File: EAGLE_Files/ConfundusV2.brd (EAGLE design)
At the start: 43.8 x 20 mm, 89 parts, among them IC1 MIC5219YM5_TR, IC2 ATTINY1616-MNR, IC4 TPS61291DRVT, J5 SM03B-SRSS-TB_LF__SN_, Q1 DMG3415U-7, Q3 DMG3415U-7, SW1 MLL1200S

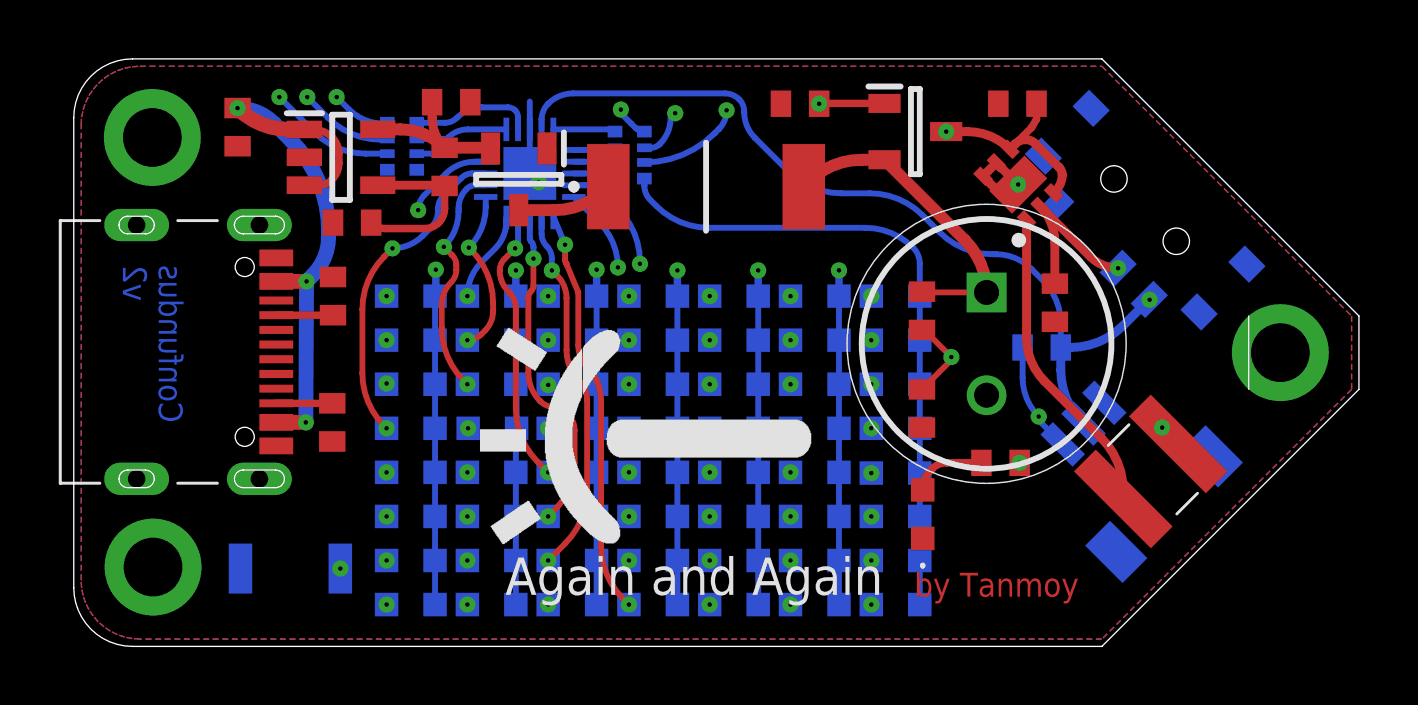
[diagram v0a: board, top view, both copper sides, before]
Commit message: Updating the circuit adjustments for introduction of a Schottky diode
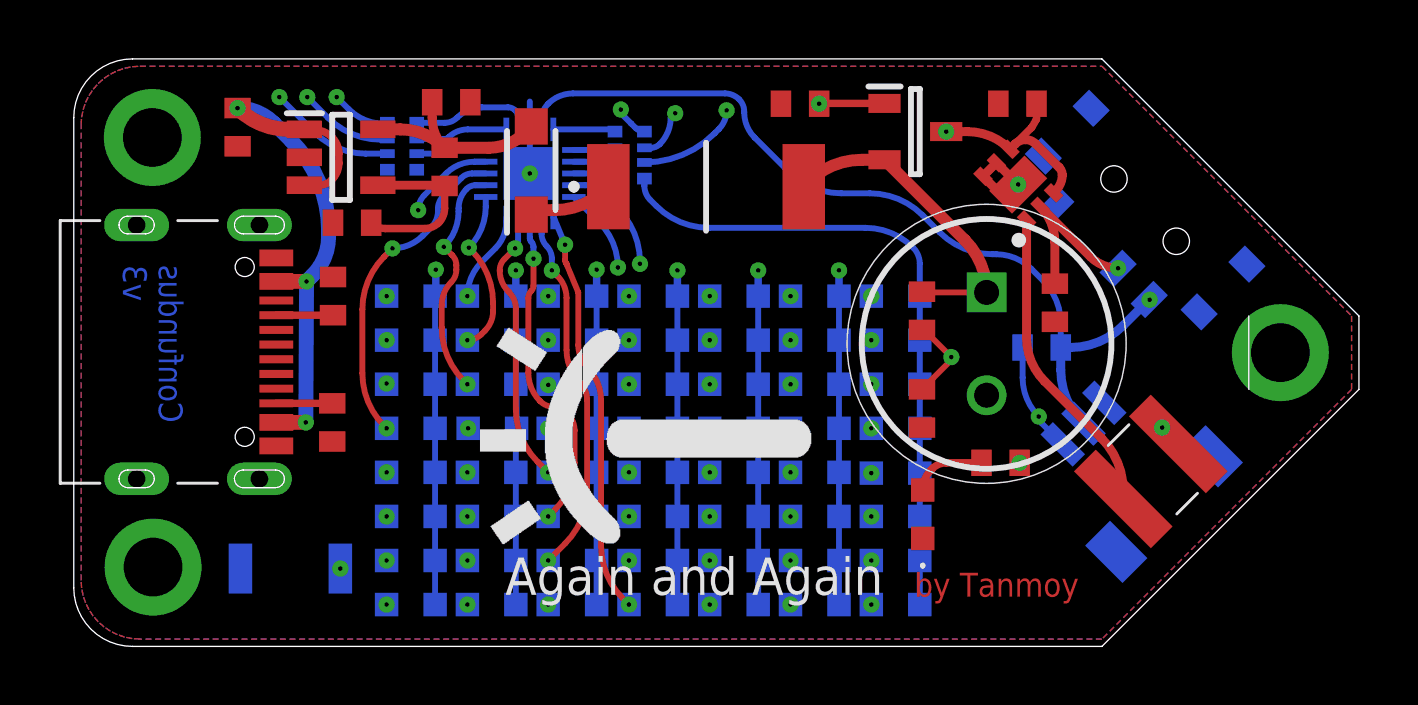
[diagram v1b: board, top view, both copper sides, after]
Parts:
- removed Q1: DMG3415U-7, DMG3415U-7:SOT96P240X100-3N
- added D1: MBR120VLSFT1G, MBR120VLSFT1G:SODFL3616X98N
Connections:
- net GND: no longer Q1.1
- net N$10: now also D1.2; no longer Q1.2
- net N$12: now also D1.1; no longer Q1.3
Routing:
- net N$10: track 5.60 -> 7.17 mm
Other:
- board text added: "Confundus v3"
- board text removed: "Confundus v2"
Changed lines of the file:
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@@
 <plain>
 <text x="3.70554375" y="12.98660625" size="0.8128" layer="16" rot="MR270">Confundus
-       v2</text>
+       v3</text>
 <text x="27.55" y="3.025" size="1.27" layer="25" rot="R180">Again and Again</text>
 <wire x1="35" y1="20" x2="2" y2="20" width="0.001" layer="20"/>
@@
 <attribute name="MOUSER_PRICE-STOCK" value="" x="9.1" y="16.65" size="1.778" layer="27" display="off"/>
 </element>
-<element name="Q1" library="DMG3415U-7" package="SOT96P240X100-3N" override_package3d_urn="urn:adsk.eagle:package:51305947/2" override_package_urn="urn:adsk.eagle:footprint:51305948/1" value="DMG3415U-7" x="15.15" y="15.9" smashed="yes" rot="R270">
-<attribute name="DESCRIPTION" value="P-CHANNEL ENHANCEMENT MODE MOSFET" x="15.15" y="15.9" size="1.778" layer="27" rot="R270" display="off"/>
-<attribute name="HEIGHT" value="1mm" x="15.15" y="15.9" size="1.778" layer="27" rot="R270" display="off"/>
-<attribute name="LCSC_PART_NUMBER" value="C96616" x="15.15" y="15.9" size="1.778" layer="27" rot="R270" display="off"/>
-<attribute name="LCSC_PRICE-STOCK" value="https://lcsc.com/product-detail/MOSFET_Diodes-Incorporated_DMG3415U-7_Diodes-Incorporated-DMG3415U-7_C96616.html" x="15.15" y="15.9" size="1.778" layer="27" rot="R270" display="off"/>
-<attribute name="MANUFACTURER_NAME" value="Diodes Inc." x="15.15" y="15.9" size="1.778" layer="27" rot="R270" display="off"/>
-<attribute name="MANUFACTURER_PART_NUMBER" value="DMG3415U-7" x="15.15" y="15.9" size="1.778" layer="27" rot="R270" display="off"/>
-</element>
 <element name="R4" library="ERJ1TYJ220U" package="ERJ1TRQF1R0U" override_package3d_urn="urn:adsk.eagle:package:52775042/2" override_package_urn="urn:adsk.eagle:footprint:52775043/1" value="ERJ1TYJ220U" x="21.525" y="15.65" smashed="yes">
 <attribute name="ARROW_PART_NUMBER" value="" x="21.525" y="15.65" size="1.778" layer="27" display="off"/>
@@
 <attribute name="MOUSER_PART_NUMBER" value="" x="21.525" y="15.65" size="1.778" layer="27" display="off"/>
 <attribute name="MOUSER_PRICE-STOCK" value="" x="21.525" y="15.65" size="1.778" layer="27" display="off"/>
+</element>
+<element name="D1" library="MBR120VLSFT1G" package="SODFL3616X98N" override_package3d_urn="urn:adsk.eagle:package:53013620/2" override_package_urn="urn:adsk.eagle:footprint:53013621/1" value="MBR120VLSFT1G" x="15.575" y="16.2" smashed="yes" rot="R90">
+<attribute name="DESCRIPTION" value="Diode Schottky 20V 1A SOD123FL ON Semi MBR120VLSFT1G, SMT Schottky Diode, 20V 1A, 2-Pin SOD-123FL" x="15.575" y="16.2" size="1.778" layer="27" rot="R90" display="off"/>
+<attribute name="HEIGHT" value="0.98mm" x="15.575" y="16.2" size="1.778" layer="27" rot="R90" display="off"/>
+<attribute name="MANUFACTURER_NAME" value="ON Semiconductor" x="15.575" y="16.2" size="1.778" layer="27" rot="R90" display="off"/>
+<attribute name="MANUFACTURER_PART_NUMBER" value="MBR120VLSFT1G" x="15.575" y="16.2" size="1.778" layer="27" rot="R90" display="off"/>
+<attribute name="MOUSER_PART_NUMBER" value="863-MBR120VLSFT1G" x="15.575" y="16.2" size="1.778" layer="27" rot="R90" display="off"/>
+<attribute name="MOUSER_PRICE-STOCK" value="https://www.mouser.co.uk/ProductDetail/ON-Semiconductor/MBR120VLSFT1G?qs=3JMERSakebpX%252BkItPpFCkg%3D%3D" x="15.575" y="16.2" size="1.778" layer="27" rot="R90" display="off"/>
 </element>
 </elements>
@@
 <contactref element="J3" pad="1"/>
 <contactref element="C10" pad="2"/>
-<via x="15.825" y="15.8" extent="1-16" drill="0.15" grouprefs="VIAS"/>
-<wire x1="15.525" y1="16.1" x2="15.825" y2="15.8" width="0.2032" layer="16"/>
+<via x="15.525" y="16.1" extent="1-16" drill="0.15" grouprefs="VIAS"/>
 <polygon width="0.1" layer="1">
 <vertex x="35" y="0.25"/>
@@
 <contactref element="IC1" pad="2"/>
 <contactref element="R2" pad="1"/>
-<contactref element="Q1" pad="1"/>
 <via x="32.15" y="15.725" extent="1-16" drill="0.15"/>
 <wire x1="32.15303125" y1="15.72196875" x2="32.15" y2="15.725" width="0.254" layer="1"/>
@@
 <contactref element="IC1" pad="5"/>
 <contactref element="C10" pad="1"/>
-<contactref element="Q1" pad="2"/>
 <contactref element="R1" pad="2"/>
 <wire x1="10.35" y1="17.6" x2="11.116115625" y2="17.6" width="0.4064" layer="1"/>
@@
 <wire x1="12.2" y1="18.001040625" x2="12.625" y2="16.975" width="0.3048" layer="1" curve="45"/>
 <wire x1="12.625" y1="16.975" x2="14.12964375" y2="16.975" width="0.4064" layer="1"/>
-<wire x1="14.12964375" y1="16.975" x2="14.19" y2="16.95" width="0.4064" layer="1" curve="-45"/>
+<contactref element="D1" pad="2"/>
+<wire x1="14.12964375" y1="16.975" x2="15.35936875" y2="17.48436875" width="0.4064" layer="1" curve="45"/>
+<wire x1="15.35936875" y1="17.48436875" x2="15.575" y2="17.7" width="0.4064" layer="1"/>
 </signal>
 <signal name="N$12">
-<contactref element="Q1" pad="3"/>
 <contactref element="R4" pad="1"/>
-<wire x1="15.15" y1="14.85" x2="16.347896875" y2="14.85" width="0.4064" layer="1"/>
-<wire x1="16.347896875" y1="14.85" x2="18.14395" y2="15.59395" width="0.4064" layer="1" curve="45"/>
+<wire x1="18.14395" y1="15.59395" x2="16.347896875" y2="14.85" width="0.4064" layer="1" curve="-45"/>
 <wire x1="18.14395" y1="15.59395" x2="18.2" y2="15.65" width="0.4064" layer="1"/>
+<contactref element="D1" pad="1"/>
+<wire x1="16.347896875" y1="14.85" x2="15.93713125" y2="14.85" width="0.4064" layer="1"/>
+<wire x1="15.93713125" y1="14.85" x2="15.575" y2="14.7" width="0.4064" layer="1" curve="45"/>
 </signal>
 </signals>
